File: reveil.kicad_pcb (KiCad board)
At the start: 2 copper layers, 170 x 90 mm, 35 parts, among them J1 Barrel_Jack_Switch, J2 AudioJack3_SwitchTR, Q1 2N3904, Q2 IRLB8721PBF, U1 MAX7219, U2 MAX7219

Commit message: Schéma/PCB : unifie D2 sur 1N5822 pour simplifier la BOM
D2 (roue libre moteur) était en 1N5819 (1A). Passe en 1N5822 (3A) pour
n'avoir qu'une seule référence de Schottky dans tout le projet : la
diode prévue pour protéger VSYS contre le retour du jack J1 (section
Alimentation du README) sera aussi une 1N5822, choisie avec de la
marge faute de datasheet pour le courant moteur réel.

Même boîtier DO-41 THT, même tension inverse (40V), même datasheet
Vishay (doc 88525, couvre déjà toute la famille 1N5817-1N5822) : seule
la Value change, schéma et PCB.

ERC/DRC revérifiés via le conteneur Docker KiBot : 0 erreur/avertissement
ERC, DRC inchangé (6 avertissements silk_edge_clearance préexistants
sur J2).

Co-Authored-By: Claude Sonnet 5 <noreply@anthropic.com>
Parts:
- D2: value 1N5819 -> 1N5822
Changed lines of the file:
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@@
 			)
 		)
-		(property "Value" "1N5819"
+		(property "Value" "1N5822"
 			(at 5.08 2.47 0)
 			(layer "F.Fab")

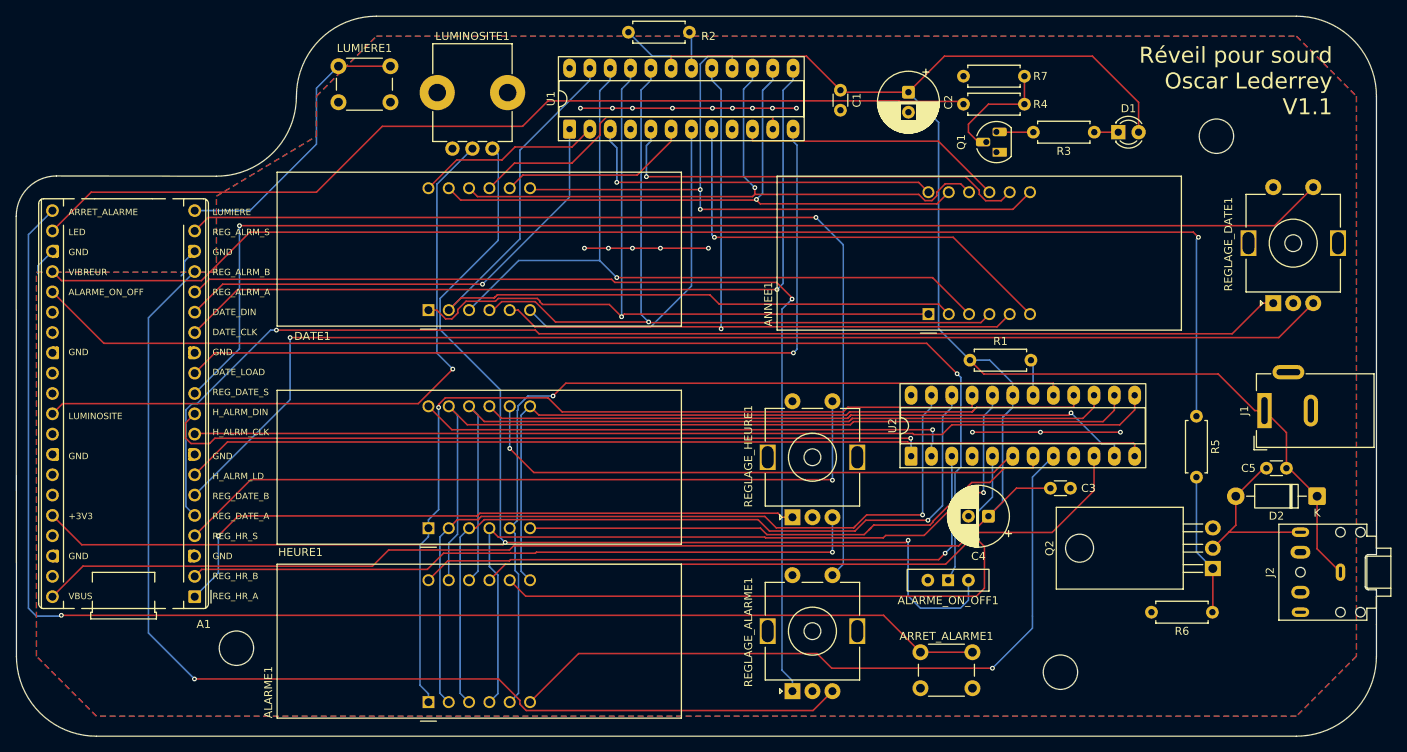
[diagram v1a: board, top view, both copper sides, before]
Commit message: Schéma/PCB : isole VBUS du jack J1, alimente le reste de la carte via VSYS
Le jack J1 alimentait directement le net VBUS, partagé avec la broche VBUS
du Pico : branché en même temps que l'USB, les deux 5 V se retrouvaient en
parallèle et le jack pouvait renvoyer du courant vers le PC.

Ajoute D3 (Schottky 1N5822, même référence que D2) entre le jack et un
nouveau rail renommé VSYS, plus C6 (220 µF) en entrée. Tout ce qui était
sur VBUS (MAX7219 U1/U2, moteur, LED, D2) passe sur VSYS, qui alimente le
Pico via sa broche VSYS (39) au lieu de VBUS (40) — VBUS reste réservé à
l'alimentation USB du Pico lui-même.

Met à jour le README (TODO alimentation + table des points de test).

Co-Authored-By: Claude Sonnet 5 <noreply@anthropic.com>
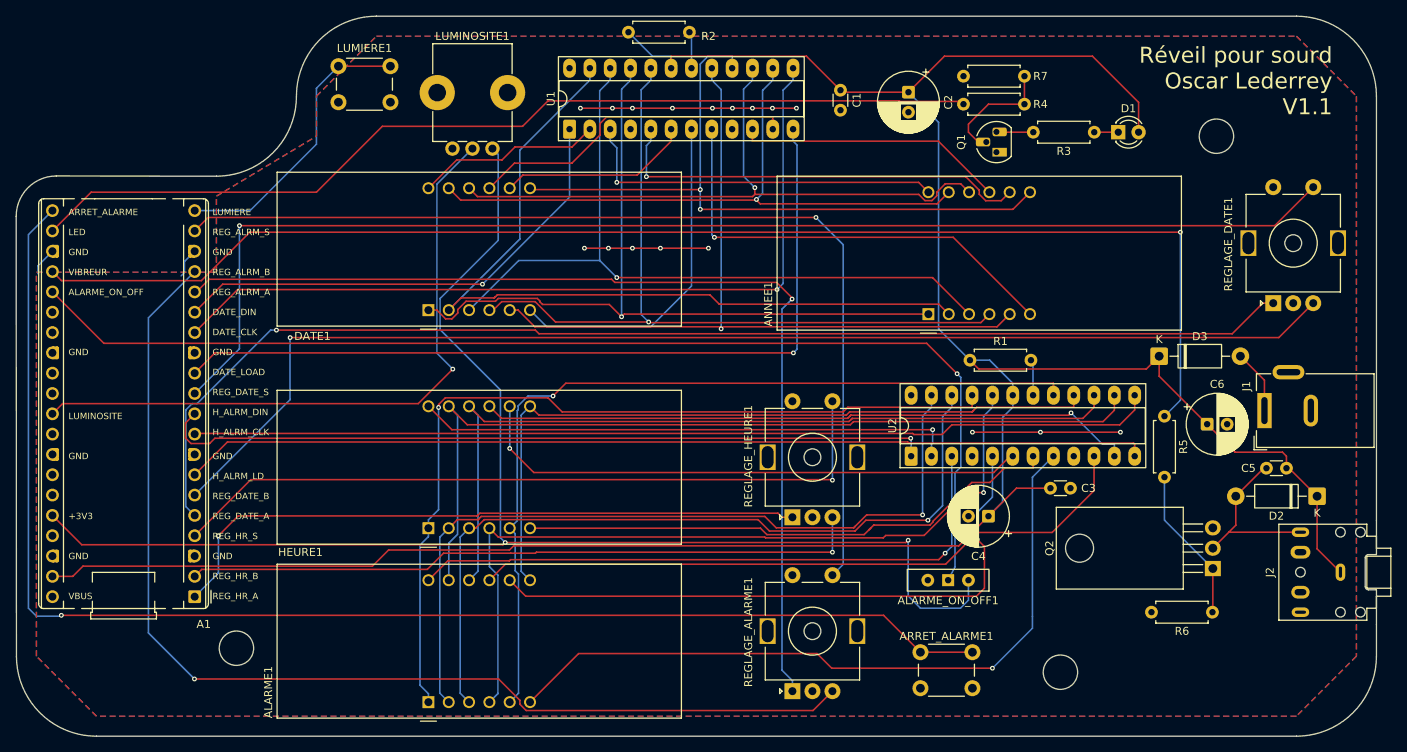
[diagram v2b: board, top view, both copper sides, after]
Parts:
- added C6: 220uF, Capacitor_THT:CP_Radial_D7.5mm_P2.50mm, F.Cu at (228.8, 71.0)
- added D3: 1N5822, Diode_THT:D_DO-41_SOD81_P10.16mm_Horizontal, F.Cu at (222.8, 62.5)
- moved R5 4.00 mm to (223.5, 70.0)
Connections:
- A1 pad 39: unconnected-(A1-VSYS-Pad39) -> VSYS
- A1 pad 40: VBUS -> unconnected-(A1-VBUS-Pad40)
- C1 pad 1: VBUS -> VSYS
- C2 pad 1: VBUS -> VSYS
- C3 pad 1: VBUS -> VSYS
- C4 pad 1: VBUS -> VSYS
- C5 pad 1: VBUS -> VSYS
- D1 pad 2: VBUS -> VSYS
- D2 pad 1: VBUS -> VSYS
- J1 pad 1: VBUS -> Net-(D3-A)
- J2 pad S: VBUS -> VSYS
- R1 pad 1: VBUS -> VSYS
- R2 pad 1: VBUS -> VSYS
- U1 pad 19: VBUS -> VSYS
- U2 pad 19: VBUS -> VSYS
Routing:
- net VSYS: track 0.00 -> 333.1 mm
- net VBUS: track 333.1 -> 0.00 mm
- net Net-(D3-A): track 0.00 -> 8.04 mm
- net Net-(Q2-G): track 17.7 -> 19.4 mm
- net VIBREUR: track 169.0 -> 167.8 mm
- added copper zone on F.Cu, net VSYS
- removed copper zone on F.Cu, net VBUS

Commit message: Schéma/PCB : découple LUMINOSITE et l'alimente depuis ADC_VREF
Ajoute C7 (100 nF) sur le curseur du potentiomètre LUMINOSITE1, et
reconnecte le haut du pont diviseur sur la broche ADC_VREF du Pico
(auparavant non connectée) au lieu de +3V3, pour une référence ADC plus
propre.

Met à jour le README : coche ce point, et marque le bouton reset et les
filtres RC des encodeurs comme des décisions explicites (pas voulus /
pas nécessaires pour l'instant) plutôt que des TODO ouverts.

Co-Authored-By: Claude Sonnet 5 <noreply@anthropic.com>
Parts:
- added C7: 100n, Capacitor_THT:C_Disc_D3.0mm_W1.6mm_P2.50mm, F.Cu at (145.5, 25.2)
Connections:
- A1 pad 35: unconnected-(A1-ADC_VREF-Pad35) -> ADC_VREF
- LUMINOSITE1 pad 1: +3V3 -> ADC_VREF
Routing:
- net ADC_VREF: track 0.00 -> 83.8 mm, vias 0 -> 1
- net +3V3: track 182.7 -> 126.8 mm, vias 2 -> 1
- net LUMINOSITE: track 82.6 -> 99.4 mm
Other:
- board text added: "RUN"
